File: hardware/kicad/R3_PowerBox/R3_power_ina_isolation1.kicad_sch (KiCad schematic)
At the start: 9 parts, among them U6 RS3-0505D/H3

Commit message: Finalize R3 PowerBox pre-routing placement
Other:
- moved on the sheet: FB4

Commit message: Rev.A review fixes: local charger power-stage reroute checkpoint
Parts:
- added R107, R108: DNP PRELOAD / BENCH SELECT, Resistor_SMD:R_2512_6332Metric, symbol R3_POWER_GEN:R
- FB4: value FB_INA_P / FB-or-0R -> 0R / FB / L BENCH SELECT; footprint Resistor_SMD:R_0805_2012Metric -> Inductor_SMD:L_1206_3216Metric_Pad1.22x1.90mm_HandSolder
- FB5: value FB_INA_N / FB-or-0R -> 0R / FB / L BENCH SELECT; footprint Resistor_SMD:R_0805_2012Metric -> Inductor_SMD:L_1206_3216Metric_Pad1.22x1.90mm_HandSolder
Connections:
- net +5V_INA: now also R107.1
- net -5V_INA: now also R108.1
- net GND_ISO: now also R107.2, R108.2
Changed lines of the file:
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@@
+	(global_label "+5V_INA"
+		(shape bidirectional)
+		(at 203.08 105 0)
+		(effects
+			(font
+				(size 0.8 0.8)
+			)
+			(justify left)
+		)
+	)
+	(global_label "GND_ISO"
+		(shape bidirectional)
+		(at 192.92 105 180)
+		(effects
+			(font
+				(size 0.8 0.8)
+			)
+			(justify right)
+		)
+	)
+	(global_label "-5V_INA"
+		(shape bidirectional)
+		(at 203.08 180 0)
+		(effects
+			(font
+				(size 0.8 0.8)
+			)
+			(justify left)
+		)
+	)
+	(global_label "GND_ISO"
+		(shape bidirectional)
+		(at 192.92 180 180)
+		(effects
+			(font
+				(size 0.8 0.8)
+			)
+			(justify right)
+		)
+	)
 	(global_label "+5V_INA"
 		(shape bidirectional)
@@
     (instances
       (project "SKiDL-Generated"
-        (path "/7d40ec76-f97b-4a90-b5ea-ddf1628062b5/d91cf1f0-873d-54fc-820a-13085f35721e"
+        (path "/2b0a7443-ac4c-4207-8273-267cee2a0847/d91cf1f0-873d-54fc-820a-13085f35721e"
           (reference "#FLG0401")
           (unit 1)))))
@@
     (instances
       (project "SKiDL-Generated"
-        (path "/7d40ec76-f97b-4a90-b5ea-ddf1628062b5/d91cf1f0-873d-54fc-820a-13085f35721e"
+        (path "/2b0a7443-ac4c-4207-8273-267cee2a0847/d91cf1f0-873d-54fc-820a-13085f35721e"
           (reference "U6")
           (unit 1)))))
@@
           (size 0.9 0.9))
         (justify left)))
-    (property "Value" "FB_INA_P / FB-or-0R"
+    (property "Value" "0R / FB / L BENCH SELECT"
       (at 155 80.54 180)
       (effects
@@
           (size 0.9 0.9))
         (justify left)))
-    (property "Footprint" "Resistor_SMD:R_0805_2012Metric"
+    (property "Footprint" "Inductor_SMD:L_1206_3216Metric_Pad1.22x1.90mm_HandSolder"
       (at 155 78 180)
       (effects
@@
     (instances
       (project "SKiDL-Generated"
-        (path "/7d40ec76-f97b-4a90-b5ea-ddf1628062b5/d91cf1f0-873d-54fc-820a-13085f35721e"
+        (path "/2b0a7443-ac4c-4207-8273-267cee2a0847/d91cf1f0-873d-54fc-820a-13085f35721e"
           (reference "FB4")
           (unit 1)))))
@@
           (size 0.9 0.9))
         (justify left)))
-    (property "Value" "FB_INA_N / FB-or-0R"
+    (property "Value" "0R / FB / L BENCH SELECT"
       (at 155 147.54 0)
       (effects
@@
           (size 0.9 0.9))
         (justify left)))
-    (property "Footprint" "Resistor_SMD:R_0805_2012Metric"
+    (property "Footprint" "Inductor_SMD:L_1206_3216Metric_Pad1.22x1.90mm_HandSolder"
       (at 155 145 0)
       (effects
@@
     (instances
       (project "SKiDL-Generated"
-        (path "/7d40ec76-f97b-4a90-b5ea-ddf1628062b5/d91cf1f0-873d-54fc-820a-13085f35721e"
+        (path "/2b0a7443-ac4c-4207-8273-267cee2a0847/d91cf1f0-873d-54fc-820a-13085f35721e"
           (reference "FB5")
           (unit 1)))))
@@
     (instances
       (project "SKiDL-Generated"
-        (path "/7d40ec76-f97b-4a90-b5ea-ddf1628062b5/d91cf1f0-873d-54fc-820a-13085f35721e"
+        (path "/2b0a7443-ac4c-4207-8273-267cee2a0847/d91cf1f0-873d-54fc-820a-13085f35721e"
           (reference "C60")
           (unit 1)))))
@@
     (instances
       (project "SKiDL-Generated"
-        (path "/7d40ec76-f97b-4a90-b5ea-ddf1628062b5/d91cf1f0-873d-54fc-820a-13085f35721e"
+        (path "/2b0a7443-ac4c-4207-8273-267cee2a0847/d91cf1f0-873d-54fc-820a-13085f35721e"
           (reference "C61")
           (unit 1)))))
@@
     (instances
       (project "SKiDL-Generated"
-        (path "/7d40ec76-f97b-4a90-b5ea-ddf1628062b5/d91cf1f0-873d-54fc-820a-13085f35721e"
+        (path "/2b0a7443-ac4c-4207-8273-267cee2a0847/d91cf1f0-873d-54fc-820a-13085f35721e"
           (reference "C62")
           (unit 1)))))
@@
     (instances
       (project "SKiDL-Generated"
-        (path "/7d40ec76-f97b-4a90-b5ea-ddf1628062b5/d91cf1f0-873d-54fc-820a-13085f35721e"
+        (path "/2b0a7443-ac4c-4207-8273-267cee2a0847/d91cf1f0-873d-54fc-820a-13085f35721e"
           (reference "C63")
+          (unit 1)))))
+  (symbol
+    (lib_id "R3_POWER_GEN:R")
+    (at 198 105 180)
+    (mirror x)
+    (unit 1)
+    (exclude_from_sim no)
+    (in_bom yes)
+    (on_board yes)
+    (dnp yes)
+    (fields_autoplaced yes)
+    (property "Reference" "R107"
+      (at 198 102.46 180)
+      (effects
+        (font
+          (size 0.9 0.9))
+        (justify left)))
+    (property "Value" "DNP PRELOAD / BENCH SELECT"
+      (at 198 107.54 180)
+      (effects
+        (font
+          (size 0.9 0.9))
+        (justify left)))
+    (property "Footprint" "Resistor_SMD:R_2512_6332Metric"
+      (at 198 105 180)
+      (effects
+        (font
+          (size 0.9 0.9))
+        (hide yes)))
+    (property "Datasheet" "~"
+      (at 198 105 180)
+      (effects
+        (font
+          (size 0.9 0.9))
+        (hide yes)))
+    (property "Description" ""
+      (at 198 105 180)
+      (effects
+        (font
+          (size 0.9 0.9))
+        (hide yes)))
+    (pin "1"
+)
+    (pin "2"
+)
+    (instances
+      (project "SKiDL-Generated"
+        (path "/2b0a7443-ac4c-4207-8273-267cee2a0847/d91cf1f0-873d-54fc-820a-13085f35721e"
+          (reference "R107")
+          (unit 1)))))
+  (symbol
+    (lib_id "R3_POWER_GEN:R")
+    (at 198 180 180)
+    (mirror x)
+    (unit 1)
+    (exclude_from_sim no)
+    (in_bom yes)
+    (on_board yes)
+    (dnp yes)
+    (fields_autoplaced yes)
+    (property "Reference" "R108"
+      (at 198 177.46 180)
+      (effects
+        (font
+          (size 0.9 0.9))
+        (justify left)))
+    (property "Value" "DNP PRELOAD / BENCH SELECT"
+      (at 198 182.54 180)
+      (effects
+        (font
+          (size 0.9 0.9))
+        (justify left)))
+    (property "Footprint" "Resistor_SMD:R_2512_6332Metric"
+      (at 198 180 180)
+      (effects
+        (font
+          (size 0.9 0.9))
+        (hide yes)))
+    (property "Datasheet" "~"
+      (at 198 180 180)
+      (effects
+        (font
+          (size 0.9 0.9))
+        (hide yes)))
+    (property "Description" ""
+      (at 198 180 180)
+      (effects
+        (font
+          (size 0.9 0.9))
+        (hide yes)))
+    (pin "1"
+)
+    (pin "2"
+)
+    (instances
+      (project "SKiDL-Generated"
+        (path "/2b0a7443-ac4c-4207-8273-267cee2a0847/d91cf1f0-873d-54fc-820a-13085f35721e"
+          (reference "R108")
           (unit 1)))))
   (symbol
@@
     (instances
       (project "SKiDL-Generated"
-        (path "/7d40ec76-f97b-4a90-b5ea-ddf1628062b5/d91cf1f0-873d-54fc-820a-13085f35721e"
+        (path "/2b0a7443-ac4c-4207-8273-267cee2a0847/d91cf1f0-873d-54fc-820a-13085f35721e"
           (reference "TP13")
           (unit 1)))))
@@
     (instances
       (project "SKiDL-Generated"
-        (path "/7d40ec76-f97b-4a90-b5ea-ddf1628062b5/d91cf1f0-873d-54fc-820a-13085f35721e"
+        (path "/2b0a7443-ac4c-4207-8273-267cee2a0847/d91cf1f0-873d-54fc-820a-13085f35721e"
           (reference "TP14")
           (unit 1)))))

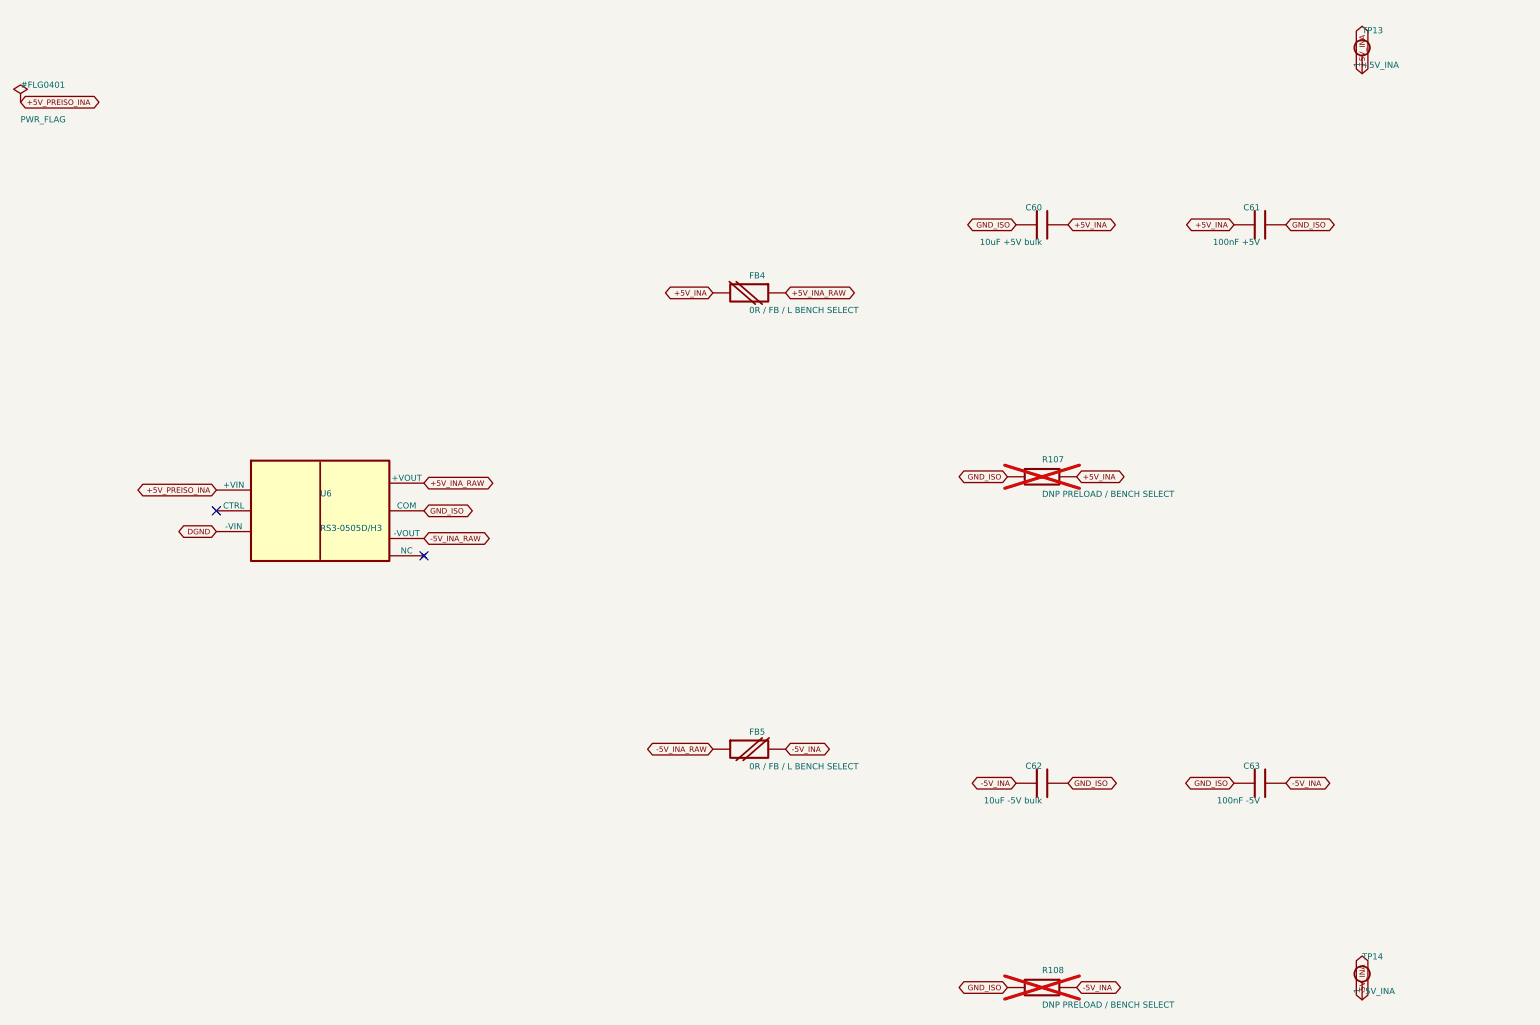
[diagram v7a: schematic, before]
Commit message: Rev.A review fixes: final CAD verification and documented hardware gates
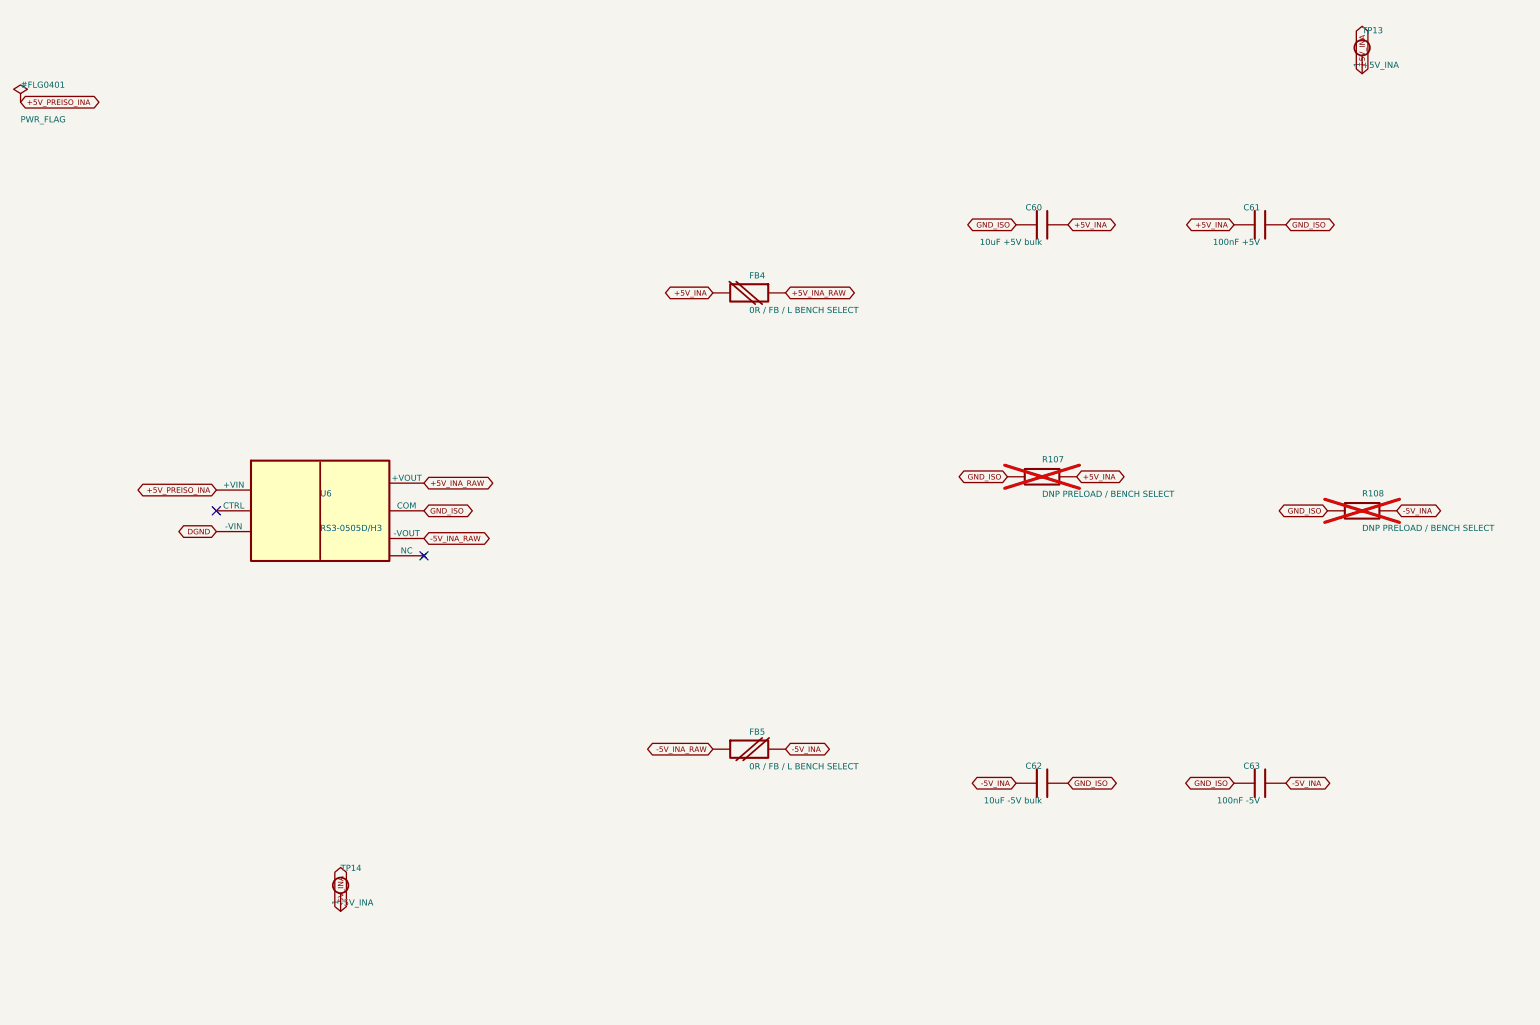
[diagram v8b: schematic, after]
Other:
- moved on the sheet: R108, TP14
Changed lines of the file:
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@@
 	(global_label "-5V_INA"
 		(shape bidirectional)
-		(at 203.08 180 0)
+		(at 250.08 110 0)
 		(effects
 			(font
@@
 	(global_label "GND_ISO"
 		(shape bidirectional)
-		(at 192.92 180 180)
+		(at 239.92 110 180)
 		(effects
 			(font
@@
 	(global_label "-5V_INA"
 		(shape bidirectional)
-		(at 245 181.81 90)
+		(at 95 168.81 90)
 		(effects
 			(font
@@
     (instances
       (project "SKiDL-Generated"
-        (path "/2b0a7443-ac4c-4207-8273-267cee2a0847/d91cf1f0-873d-54fc-820a-13085f35721e"
+        (path "/9d9979b9-42ef-4da5-ae7f-11c414f8c896/d91cf1f0-873d-54fc-820a-13085f35721e"
           (reference "#FLG0401")
           (unit 1)))))
@@
     (instances
       (project "SKiDL-Generated"
-        (path "/2b0a7443-ac4c-4207-8273-267cee2a0847/d91cf1f0-873d-54fc-820a-13085f35721e"
+        (path "/9d9979b9-42ef-4da5-ae7f-11c414f8c896/d91cf1f0-873d-54fc-820a-13085f35721e"
           (reference "U6")
           (unit 1)))))
@@
     (instances
       (project "SKiDL-Generated"
-        (path "/2b0a7443-ac4c-4207-8273-267cee2a0847/d91cf1f0-873d-54fc-820a-13085f35721e"
+        (path "/9d9979b9-42ef-4da5-ae7f-11c414f8c896/d91cf1f0-873d-54fc-820a-13085f35721e"
           (reference "FB4")
           (unit 1)))))
@@
     (instances
       (project "SKiDL-Generated"
-        (path "/2b0a7443-ac4c-4207-8273-267cee2a0847/d91cf1f0-873d-54fc-820a-13085f35721e"
+        (path "/9d9979b9-42ef-4da5-ae7f-11c414f8c896/d91cf1f0-873d-54fc-820a-13085f35721e"
           (reference "FB5")
           (unit 1)))))
@@
     (instances
       (project "SKiDL-Generated"
-        (path "/2b0a7443-ac4c-4207-8273-267cee2a0847/d91cf1f0-873d-54fc-820a-13085f35721e"
+        (path "/9d9979b9-42ef-4da5-ae7f-11c414f8c896/d91cf1f0-873d-54fc-820a-13085f35721e"
           (reference "C60")
           (unit 1)))))
@@
     (instances
       (project "SKiDL-Generated"
-        (path "/2b0a7443-ac4c-4207-8273-267cee2a0847/d91cf1f0-873d-54fc-820a-13085f35721e"
+        (path "/9d9979b9-42ef-4da5-ae7f-11c414f8c896/d91cf1f0-873d-54fc-820a-13085f35721e"
           (reference "C61")
           (unit 1)))))
@@
     (instances
       (project "SKiDL-Generated"
-        (path "/2b0a7443-ac4c-4207-8273-267cee2a0847/d91cf1f0-873d-54fc-820a-13085f35721e"
+        (path "/9d9979b9-42ef-4da5-ae7f-11c414f8c896/d91cf1f0-873d-54fc-820a-13085f35721e"
           (reference "C62")
           (unit 1)))))
@@
     (instances
       (project "SKiDL-Generated"
-        (path "/2b0a7443-ac4c-4207-8273-267cee2a0847/d91cf1f0-873d-54fc-820a-13085f35721e"
+        (path "/9d9979b9-42ef-4da5-ae7f-11c414f8c896/d91cf1f0-873d-54fc-820a-13085f35721e"
           (reference "C63")
           (unit 1)))))
@@
     (instances
       (project "SKiDL-Generated"
-        (path "/2b0a7443-ac4c-4207-8273-267cee2a0847/d91cf1f0-873d-54fc-820a-13085f35721e"
+        (path "/9d9979b9-42ef-4da5-ae7f-11c414f8c896/d91cf1f0-873d-54fc-820a-13085f35721e"
           (reference "R107")
           (unit 1)))))
   (symbol
     (lib_id "R3_POWER_GEN:R")
-    (at 198 180 180)
+    (at 245 110 180)
     (mirror x)
     (unit 1)
@@
     (fields_autoplaced yes)
     (property "Reference" "R108"
-      (at 198 177.46 180)
+      (at 245 107.46 180)
       (effects
         (font
@@
         (justify left)))
     (property "Value" "DNP PRELOAD / BENCH SELECT"
-      (at 198 182.54 180)
+      (at 245 112.54 180)
       (effects
         (font
@@
         (justify left)))
     (property "Footprint" "Resistor_SMD:R_2512_6332Metric"
-      (at 198 180 180)
-      (effects
-        (font
-          (size 0.9 0.9))
-        (hide yes)))
-    (property "Datasheet" "~"
-      (at 198 180 180)
-      (effects
-        (font
-          (size 0.9 0.9))
-        (hide yes)))
-    (property "Description" ""
-      (at 198 180 180)
-      (effects
-        (font
-          (size 0.9 0.9))
-        (hide yes)))
-    (pin "1"
-)
-    (pin "2"
-)
-    (instances
-      (project "SKiDL-Generated"
-        (path "/2b0a7443-ac4c-4207-8273-267cee2a0847/d91cf1f0-873d-54fc-820a-13085f35721e"
+      (at 245 110 180)
+      (effects
+        (font
+          (size 0.9 0.9))
+        (hide yes)))
+    (property "Datasheet" "~"
+      (at 245 110 180)
+      (effects
+        (font
+          (size 0.9 0.9))
+        (hide yes)))
+    (property "Description" ""
+      (at 245 110 180)
+      (effects
+        (font
+          (size 0.9 0.9))
+        (hide yes)))
+    (pin "1"
+)
+    (pin "2"
+)
+    (instances
+      (project "SKiDL-Generated"
+        (path "/9d9979b9-42ef-4da5-ae7f-11c414f8c896/d91cf1f0-873d-54fc-820a-13085f35721e"
           (reference "R108")
           (unit 1)))))
@@
     (instances
       (project "SKiDL-Generated"
-        (path "/2b0a7443-ac4c-4207-8273-267cee2a0847/d91cf1f0-873d-54fc-820a-13085f35721e"
+        (path "/9d9979b9-42ef-4da5-ae7f-11c414f8c896/d91cf1f0-873d-54fc-820a-13085f35721e"
           (reference "TP13")
           (unit 1)))))
   (symbol
     (lib_id "R3_POWER_GEN:TP")
-    (at 245 178 0)
+    (at 95 165 0)
     (unit 1)
     (exclude_from_sim no)
@@
     (fields_autoplaced yes)
     (property "Reference" "TP14"
-      (at 245 175.46 0)
+      (at 95 162.46 0)
       (effects
         (font
@@
         (justify left)))
     (property "Value" "-5V_INA"
-      (at 245 180.54 0)
+      (at 95 167.54 0)
       (effects
         (font
@@
         (justify left)))
     (property "Footprint" "TestPoint:TestPoint_Plated_Hole_D2.0mm"
-      (at 245 178 0)
-      (effects
-        (font
-          (size 0.9 0.9))
-        (hide yes)))
-    (property "Datasheet" "~"
-      (at 245 178 0)
-      (effects
-        (font
-          (size 0.9 0.9))
-        (hide yes)))
-    (property "Description" ""
-      (at 245 178 0)
-      (effects
-        (font
-          (size 0.9 0.9))
-        (hide yes)))
-    (pin "1"
-)
-    (instances
-      (project "SKiDL-Generated"
-        (path "/2b0a7443-ac4c-4207-8273-267cee2a0847/d91cf1f0-873d-54fc-820a-13085f35721e"
+      (at 95 165 0)
+      (effects
+        (font
+          (size 0.9 0.9))
+        (hide yes)))
+    (property "Datasheet" "~"
+      (at 95 165 0)
+      (effects
+        (font
+          (size 0.9 0.9))
+        (hide yes)))
+    (property "Description" ""
+      (at 95 165 0)
+      (effects
+        (font
+          (size 0.9 0.9))
+        (hide yes)))
+    (pin "1"
+)
+    (instances
+      (project "SKiDL-Generated"
+        (path "/9d9979b9-42ef-4da5-ae7f-11c414f8c896/d91cf1f0-873d-54fc-820a-13085f35721e"
           (reference "TP14")
           (unit 1)))))
